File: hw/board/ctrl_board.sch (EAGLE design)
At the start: 27 parts, among them IC1 7805T

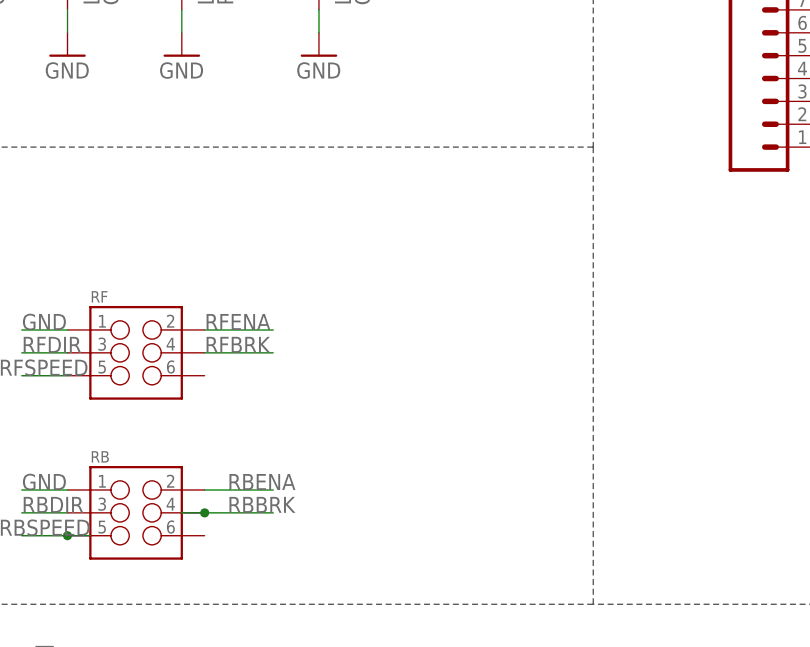
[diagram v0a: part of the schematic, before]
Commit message: Added power connectors to ctrl board, fix pwr board error
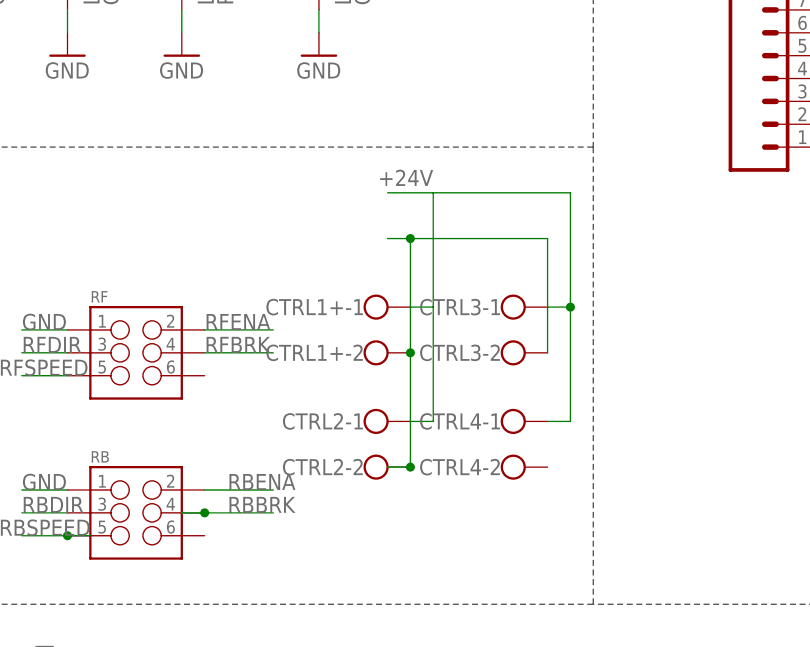
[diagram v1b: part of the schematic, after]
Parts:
- added CTRL1+, CTRL2, CTRL3, CTRL4: (no value), con-wago-500:W237-102
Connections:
- new net N$2: CTRL1+-1.KL, CTRL2-1.KL
- net +24V: now also CTRL3-1.KL, CTRL4-1.KL
- net GND: now also CTRL1+-2.KL, CTRL2-2.KL, CTRL3-2.KL
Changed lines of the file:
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@@
 <part name="TO_PWRBRD_SINGNALS" library="SparkFun-Connectors" deviceset="M03X2" device="POGO_PINS"/>
 <part name="TO_PWRBRD_PWR" library="con-wago-500" deviceset="W237-102" device=""/>
+<part name="CTRL1+" library="con-wago-500" deviceset="W237-102" device=""/>
+<part name="CTRL3" library="con-wago-500" deviceset="W237-102" device=""/>
+<part name="CTRL2" library="con-wago-500" deviceset="W237-102" device=""/>
+<part name="CTRL4" library="con-wago-500" deviceset="W237-102" device=""/>
 </parts>
 <sheets>
@@
 <instance part="TO_PWRBRD_PWR" gate="-1" x="373.38" y="142.24"/>
 <instance part="TO_PWRBRD_PWR" gate="-2" x="373.38" y="134.62"/>
+<instance part="CTRL1+" gate="-1" x="78.74" y="104.14"/>
+<instance part="CTRL1+" gate="-2" x="78.74" y="99.06"/>
+<instance part="CTRL3" gate="-1" x="93.98" y="104.14"/>
+<instance part="CTRL3" gate="-2" x="93.98" y="99.06"/>
+<instance part="CTRL2" gate="-1" x="78.74" y="91.44"/>
+<instance part="CTRL2" gate="-2" x="78.74" y="86.36"/>
+<instance part="CTRL4" gate="-1" x="93.98" y="91.44"/>
+<instance part="CTRL4" gate="-2" x="93.98" y="86.36"/>
 </instances>
 <busses>
@@
 <wire x1="378.46" y1="134.62" x2="388.62" y2="134.62" width="0.1524" layer="91"/>
 </segment>
+<segment>
+<pinref part="CTRL1+" gate="-2" pin="KL"/>
+<wire x1="81.28" y1="111.76" x2="83.82" y2="111.76" width="0.1524" layer="91"/>
+<wire x1="83.82" y1="111.76" x2="83.82" y2="99.06" width="0.1524" layer="91"/>
+<pinref part="CTRL2" gate="-2" pin="KL"/>
+<wire x1="83.82" y1="99.06" x2="83.82" y2="86.36" width="0.1524" layer="91"/>
+<junction x="83.82" y="99.06"/>
+<wire x1="83.82" y1="86.36" x2="81.28" y2="86.36" width="0.1524" layer="91"/>
+<junction x="83.82" y="86.36"/>
+<wire x1="83.82" y1="111.76" x2="99.06" y2="111.76" width="0.1524" layer="91"/>
+<junction x="83.82" y="111.76"/>
+<pinref part="CTRL3" gate="-2" pin="KL"/>
+<wire x1="99.06" y1="111.76" x2="99.06" y2="99.06" width="0.1524" layer="91"/>
+</segment>
 </net>
 <net name="DIO4" class="0">
@@
 <wire x1="378.46" y1="142.24" x2="388.62" y2="142.24" width="0.1524" layer="91"/>
 </segment>
+<segment>
+<wire x1="81.28" y1="116.84" x2="101.6" y2="116.84" width="0.1524" layer="91"/>
+<wire x1="101.6" y1="116.84" x2="101.6" y2="104.14" width="0.1524" layer="91"/>
+<pinref part="CTRL3" gate="-1" pin="KL"/>
+<wire x1="101.6" y1="104.14" x2="99.06" y2="104.14" width="0.1524" layer="91"/>
+<wire x1="101.6" y1="104.14" x2="101.6" y2="91.44" width="0.1524" layer="91"/>
+<junction x="101.6" y="104.14"/>
+<pinref part="CTRL4" gate="-1" pin="KL"/>
+<wire x1="101.6" y1="91.44" x2="99.06" y2="91.44" width="0.1524" layer="91"/>
+<label x="86.36" y="119.38" size="1.778" layer="95" rot="R180"/>
+</segment>
 </net>
 <net name="READ_CAP" class="0">
@@
 </segment>
 </net>
+<net name="N$2" class="0">
+<segment>
+<pinref part="CTRL1+" gate="-1" pin="KL"/>
+<wire x1="83.82" y1="104.14" x2="86.36" y2="104.14" width="0.1524" layer="91"/>
+<wire x1="86.36" y1="104.14" x2="86.36" y2="116.84" width="0.1524" layer="91"/>
+<wire x1="86.36" y1="104.14" x2="86.36" y2="91.44" width="0.1524" layer="91"/>
+<pinref part="CTRL2" gate="-1" pin="KL"/>
+<wire x1="86.36" y1="91.44" x2="83.82" y2="91.44" width="0.1524" layer="91"/>
+</segment>
+</net>
